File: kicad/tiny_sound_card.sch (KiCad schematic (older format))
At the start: 45 parts, among them CON1 BARREL_JACK, IC1 ATMEGA328P-A, J1 TRS_JACK, M1 DFR0299, P1 EXT_PWR, P2 SPKOUT, P3 EXT_SW0, P4 EXT_I2C, P5 EXT_SW1, P6 EXT_UART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

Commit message: LEDのポートを変更
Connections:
- net D13: no longer R2.1
- net D2: now also R2.1
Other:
- moved on the sheet: D1, R2
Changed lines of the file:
@@
 L LED D1
 U 1 1 5B795926
-P 4500 4100
-F 0 "D1" H 4350 4150 50  0000 C CNN
-F 1 "LED" H 4500 4000 50  0000 C CNN
-F 2 "LEDs:LED_D3.0mm" H 4000 4050 50  0001 C CNN
-F 3 "" H 4500 4100 50  0000 C CNN
-	1    4500 4100
+P 4200 5400
+F 0 "D1" H 4050 5450 50  0000 C CNN
+F 1 "LED" H 4200 5300 50  0000 C CNN
+F 2 "LEDs:LED_D3.0mm" H 3700 5350 50  0001 C CNN
+F 3 "" H 4200 5400 50  0000 C CNN
+	1    4200 5400
 	-1   0    0    1
 $EndComp
@@
 L GND #PWR09
 U 1 1 5B7959AE
-P 4850 4100
-F 0 "#PWR09" H 4850 3850 50  0001 C CNN
-F 1 "GND" H 4850 3950 50  0000 C CNN
-F 2 "" H 4850 4100 50  0000 C CNN
-F 3 "" H 4850 4100 50  0000 C CNN
-	1    4850 4100
+P 4550 5400
+F 0 "#PWR09" H 4550 5150 50  0001 C CNN
+F 1 "GND" H 4550 5250 50  0000 C CNN
+F 2 "" H 4550 5400 50  0000 C CNN
+F 3 "" H 4550 5400 50  0000 C CNN
+	1    4550 5400
 	1    0    0    -1
 $EndComp
 Wire Wire Line
-	4700 4100 4850 4100
+	4400 5400 4550 5400
 Wire Wire Line
-	3450 4100 3950 4100
+	3450 4100 3700 4100
 Wire Wire Line
-	4250 4100 4300 4100
+	3950 5400 4000 5400
 Text Label 3700 3700 0    60   ~ 0
 ATMEGA_TX
@@
 	5300 6100 5250 6100
 Wire Wire Line
-	5250 6100 5250 6300
+	5250 6300 5250 6100
 Wire Wire Line
 	5250 6200 5300 6200
 Wire Wire Line
-	5250 6300 4800 6300
+	4800 6300 5250 6300
 Connection ~ 5050 6300
 Connection ~ 5250 6200
@@
 L R R2
 U 1 1 5B79BCA9
-P 4100 4100
-F 0 "R2" V 4180 4100 50  0000 C CNN
-F 1 "10k" V 4100 4100 50  0000 C CNN
-F 2 "Resistors_ThroughHole:R_Axial_DIN0207_L6.3mm_D2.5mm_P10.16mm_Horizontal" V 4030 4100 50  0001 C CNN
-F 3 "" H 4100 4100 50  0000 C CNN
-	1    4100 4100
+P 3800 5400
+F 0 "R2" V 3880 5400 50  0000 C CNN
+F 1 "10k" V 3800 5400 50  0000 C CNN
+F 2 "Resistors_ThroughHole:R_Axial_DIN0207_L6.3mm_D2.5mm_P10.16mm_Horizontal" V 3730 5400 50  0001 C CNN
+F 3 "" H 3800 5400 50  0000 C CNN
+	1    3800 5400
 	0    -1   -1   0
 $EndComp

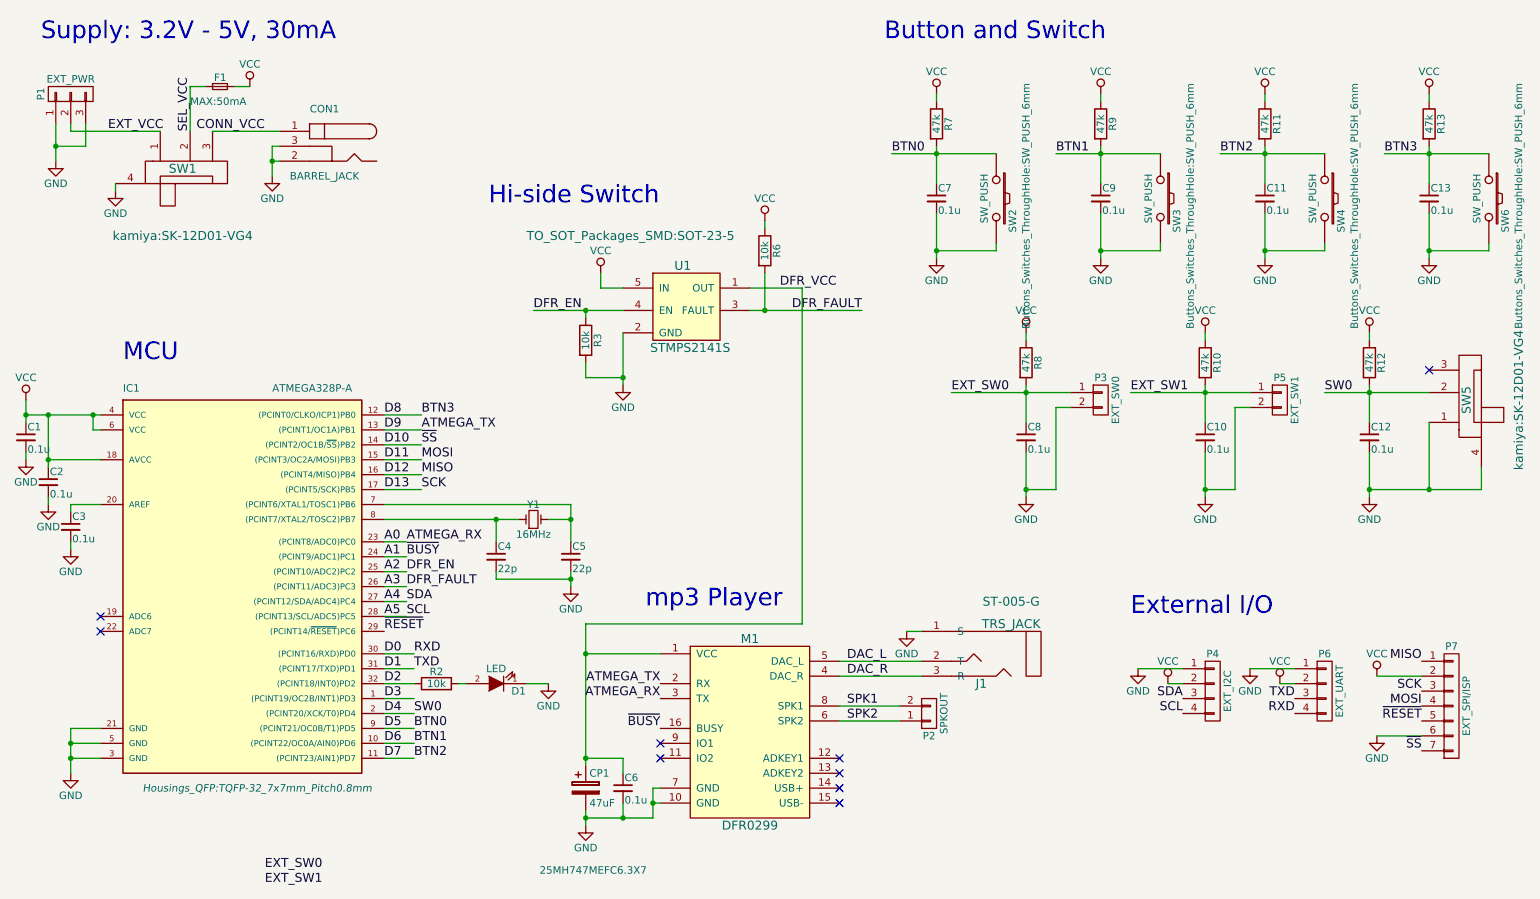
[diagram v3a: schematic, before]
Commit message: EXT_SW1を削除
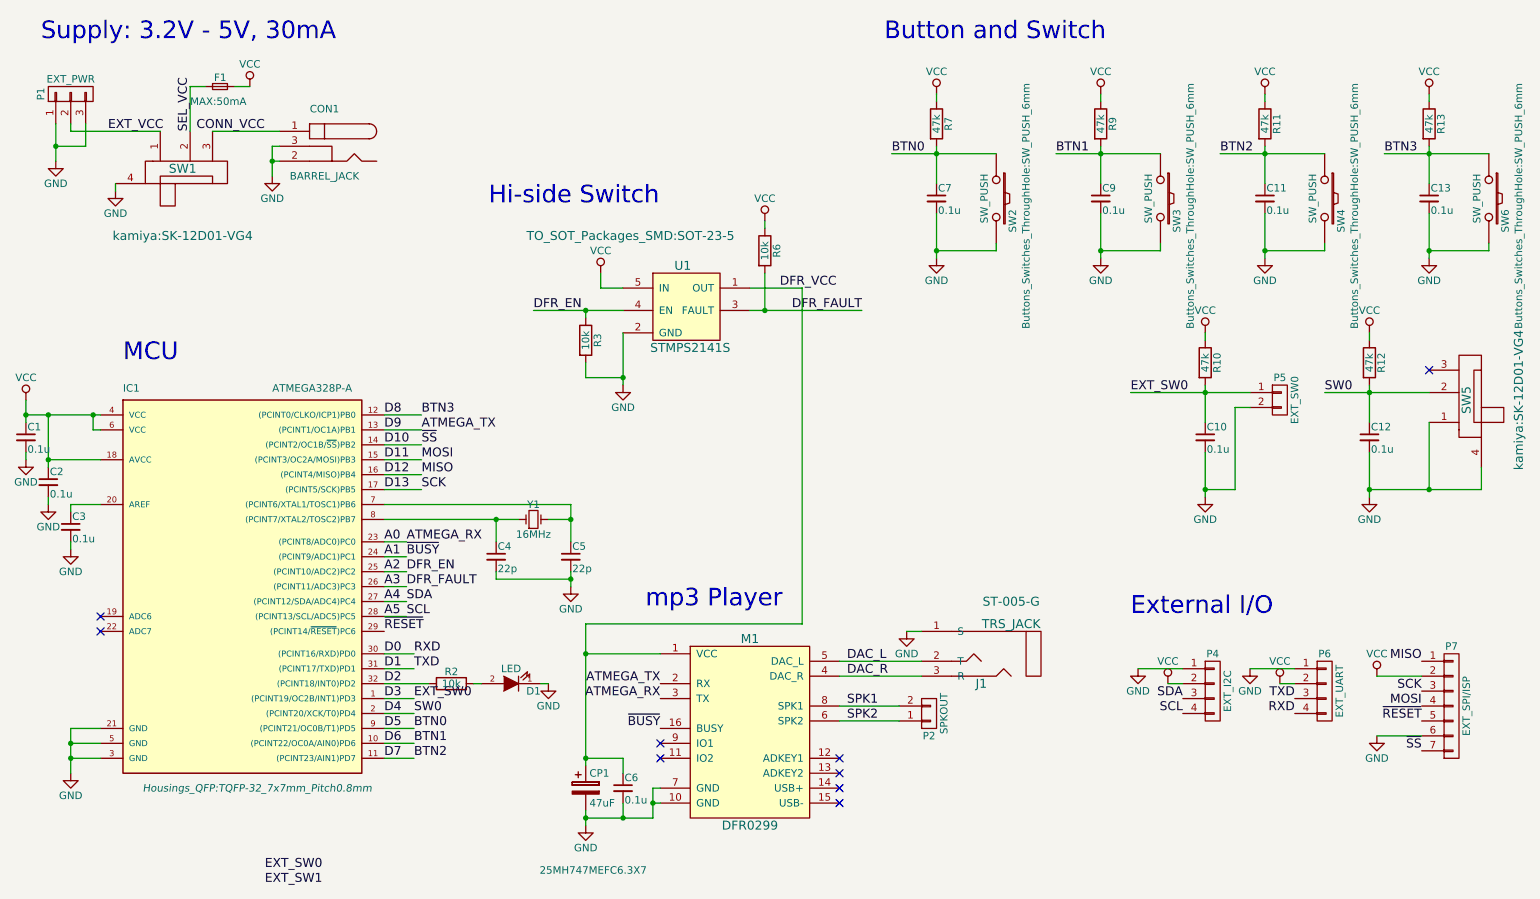
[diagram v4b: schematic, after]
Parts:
- removed C8: 0.1u, Capacitors_ThroughHole:C_Disc_D3.8mm_W2.6mm_P2.50mm, symbol C_Small
- removed P3: EXT_SW0, Pin_Headers:Pin_Header_Angled_1x02_Pitch2.54mm, symbol CONN_01X02
- removed R8: 47k, Resistors_ThroughHole:R_Axial_DIN0207_L6.3mm_D2.5mm_P10.16mm_Horizontal, symbol R
- P5: value EXT_SW1 -> EXT_SW0
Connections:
- net D3: now also C10.1, P5.1 (P1), R10.2
- net EXT_SW1: no longer C10.1, P5.1 (P1), R10.2
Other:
- moved on the sheet: D1, R2
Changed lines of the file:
@@
 L LED D1
 U 1 1 5B795926
-P 4200 5400
-F 0 "D1" H 4050 5450 50  0000 C CNN
-F 1 "LED" H 4200 5300 50  0000 C CNN
-F 2 "LEDs:LED_D3.0mm" H 3700 5350 50  0001 C CNN
-F 3 "" H 4200 5400 50  0000 C CNN
-	1    4200 5400
+P 4300 5400
+F 0 "D1" H 4150 5450 50  0000 C CNN
+F 1 "LED" H 4300 5300 50  0000 C CNN
+F 2 "LEDs:LED_D3.0mm" H 3800 5350 50  0001 C CNN
+F 3 "" H 4300 5400 50  0000 C CNN
+	1    4300 5400
 	-1   0    0    1
 $EndComp
@@
 $EndComp
 Wire Wire Line
-	4400 5400 4550 5400
+	4500 5400 4550 5400
 Wire Wire Line
 	3450 4100 3700 4100
 Wire Wire Line
-	3950 5400 4000 5400
+	4050 5400 4100 5400
 Text Label 3700 3700 0    60   ~ 0
 ATMEGA_TX
@@
 L R R2
 U 1 1 5B79BCA9
-P 3800 5400
-F 0 "R2" V 3880 5400 50  0000 C CNN
-F 1 "10k" V 3800 5400 50  0000 C CNN
-F 2 "Resistors_ThroughHole:R_Axial_DIN0207_L6.3mm_D2.5mm_P10.16mm_Horizontal" V 3730 5400 50  0001 C CNN
-F 3 "" H 3800 5400 50  0000 C CNN
-	1    3800 5400
+P 3900 5400
+F 0 "R2" V 3980 5400 50  0000 C CNN
+F 1 "10k" V 3900 5400 50  0000 C CNN
+F 2 "Resistors_ThroughHole:R_Axial_DIN0207_L6.3mm_D2.5mm_P10.16mm_Horizontal" V 3830 5400 50  0001 C CNN
+F 3 "" H 3900 5400 50  0000 C CNN
+	1    3900 5400
 	0    -1   -1   0
 $EndComp
@@
 EXT_SW1
 Text Label 8450 3450 0    60   ~ 0
-EXT_SW1
+EXT_SW0
 $Comp
 L R R10
@@
 P 9450 3500
 F 0 "P5" H 9450 3650 50  0000 C CNN
-F 1 "EXT_SW1" V 9550 3500 50  0000 C CNN
+F 1 "EXT_SW0" V 9550 3500 50  0000 C CNN
 F 2 "Pin_Headers:Pin_Header_Angled_1x02_Pitch2.54mm" H 9450 3500 50  0001 C CNN
 F 3 "" H 9450 3500 50  0000 C CNN
@@
 	9150 4100 8950 4100
 Connection ~ 8950 4100
-Text Label 7250 3450 0    60   ~ 0
-EXT_SW0
-$Comp
-L R R8
-U 1 1 5B7A4031
-P 7750 3250
-F 0 "R8" V 7830 3250 50  0000 C CNN
-F 1 "47k" V 7750 3250 50  0000 C CNN
-F 2 "Resistors_ThroughHole:R_Axial_DIN0207_L6.3mm_D2.5mm_P10.16mm_Horizontal" V 7680 3250 50  0001 C CNN
-F 3 "" H 7750 3250 50  0000 C CNN
-	1    7750 3250
-	1    0    0    -1
-$EndComp
-$Comp
-L C_Small C8
-U 1 1 5B7A4037
-P 7750 3750
-F 0 "C8" H 7760 3820 50  0000 L CNN
-F 1 "0.1u" H 7760 3670 50  0000 L CNN
-F 2 "Capacitors_ThroughHole:C_Disc_D3.8mm_W2.6mm_P2.50mm" H 7750 3750 50  0001 C CNN
-F 3 "" H 7750 3750 50  0000 C CNN
-	1    7750 3750
-	1    0    0    -1
-$EndComp
-$Comp
-L VCC #PWR029
-U 1 1 5B7A403D
-P 7750 3050
-F 0 "#PWR029" H 7750 2900 50  0001 C CNN
-F 1 "VCC" H 7750 3200 50  0000 C CNN
-F 2 "" H 7750 3050 50  0000 C CNN
-F 3 "" H 7750 3050 50  0000 C CNN
-	1    7750 3050
-	1    0    0    -1
-$EndComp
-Wire Wire Line
-	7750 3050 7750 3100
-Wire Wire Line
-	7750 3400 7750 3650
-Wire Wire Line
-	7250 3450 8050 3450
-Connection ~ 7750 3450
-Wire Wire Line
-	7750 3850 7750 4150
-$Comp
-L GND #PWR030
-U 1 1 5B7A4048
-P 7750 4150
-F 0 "#PWR030" H 7750 3900 50  0001 C CNN
-F 1 "GND" H 7750 4000 50  0000 C CNN
-F 2 "" H 7750 4150 50  0000 C CNN
-F 3 "" H 7750 4150 50  0000 C CNN
-	1    7750 4150
-	1    0    0    -1
-$EndComp
-$Comp
-L CONN_01X02 P3
-U 1 1 5B7A404E
-P 8250 3500
-F 0 "P3" H 8250 3650 50  0000 C CNN
-F 1 "EXT_SW0" V 8350 3500 50  0000 C CNN
-F 2 "Pin_Headers:Pin_Header_Angled_1x02_Pitch2.54mm" H 8250 3500 50  0001 C CNN
-F 3 "" H 8250 3500 50  0000 C CNN
-	1    8250 3500
-	1    0    0    -1
-$EndComp
-Wire Wire Line
-	8050 3550 7950 3550
-Wire Wire Line
-	7950 3550 7950 4100
-Wire Wire Line
-	7950 4100 7750 4100
-Connection ~ 7750 4100
 Wire Wire Line
 	3450 3800 3700 3800
@@
 $EndComp
 $Comp
-L GND #PWR031
+L GND #PWR029
 U 1 1 5B7A8306
 P 8500 5300
-F 0 "#PWR031" H 8500 5050 50  0001 C CNN
+F 0 "#PWR029" H 8500 5050 50  0001 C CNN
 F 1 "GND" H 8500 5150 50  0000 C CNN
 F 2 "" H 8500 5300 50  0000 C CNN
@@
 $EndComp
 $Comp
-L VCC #PWR032
+L VCC #PWR030
 U 1 1 5B7A86A9
 P 8700 5400
-F 0 "#PWR032" H 8700 5250 50  0001 C CNN
+F 0 "#PWR030" H 8700 5250 50  0001 C CNN
 F 1 "VCC" H 8700 5550 50  0000 C CNN
 F 2 "" H 8700 5400 50  0000 C CNN
@@
 $EndComp
 $Comp
-L GND #PWR033
+L GND #PWR031
 U 1 1 5B7AA8F9
 P 9250 5300
-F 0 "#PWR033" H 9250 5050 50  0001 C CNN
+F 0 "#PWR031" H 9250 5050 50  0001 C CNN
 F 1 "GND" H 9250 5150 50  0000 C CNN
 F 2 "" H 9250 5300 50  0000 C CNN
@@
 $EndComp
 $Comp
-L VCC #PWR034
+L VCC #PWR032
 U 1 1 5B7AA8FF
 P 9450 5400
-F 0 "#PWR034" H 9450 5250 50  0001 C CNN
+F 0 "#PWR032" H 9450 5250 50  0001 C CNN
 F 1 "VCC" H 9450 5550 50  0000 C CNN
 F 2 "" H 9450 5400 50  0000 C CNN
@@
 	9450 5400 9550 5400
 $Comp
-L VCC #PWR035
+L VCC #PWR033
 U 1 1 5B7AAB9D
 P 10100 5350
-F 0 "#PWR035" H 10100 5200 50  0001 C CNN
+F 0 "#PWR033" H 10100 5200 50  0001 C CNN
 F 1 "VCC" H 10100 5500 50  0000 C CNN
 F 2 "" H 10100 5350 50  0000 C CNN
@@
 ~RESET
 $Comp
-L GND #PWR036
+L GND #PWR034
 U 1 1 5B7B7DEC
 P 10100 5750
-F 0 "#PWR036" H 10100 5500 50  0001 C CNN
+F 0 "#PWR034" H 10100 5500 50  0001 C CNN
 F 1 "GND" H 10100 5600 50  0000 C CNN
 F 2 "" H 10100 5750 50  0000 C CNN
@@
 DFR_EN
 Wire Wire Line
-	3450 5400 3650 5400
+	3450 5400 3750 5400
 Wire Wire Line
 	3450 5500 3650 5500
@@
 Text Label 3600 4750 0    60   ~ 0
 DFR_FAULT
+Text Label 3650 5500 0    60   ~ 0
+EXT_SW0
 $EndSCHEMATC

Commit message: Close #1
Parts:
- added R1, R4: 1k, Resistors_ThroughHole:R_Axial_DIN0207_L6.3mm_D2.5mm_P10.16mm_Horizontal, symbol R
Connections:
- net A0: now also R4.1; no longer M1.3 (TX)
- net ATMEGA_TX: now also R1.2; no longer IC1.13 ((PCINT1/OC1A)PB1)
- new net: M1.3 (TX), R4.2
- new net D9: IC1.13 ((PCINT1/OC1A)PB1), R1.1
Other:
- moved on the sheet: D1
